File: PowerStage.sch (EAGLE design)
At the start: 97 parts, among them IC1 FSBB30CH60, IC2 HCNR200, IC4 LM358D, IC5 HCNR200, IC6 78L05F, Q1 BC817-16SMD, X1 MKDSN1,5/2-5,08, X2 MKDSN1,5/3-5,08

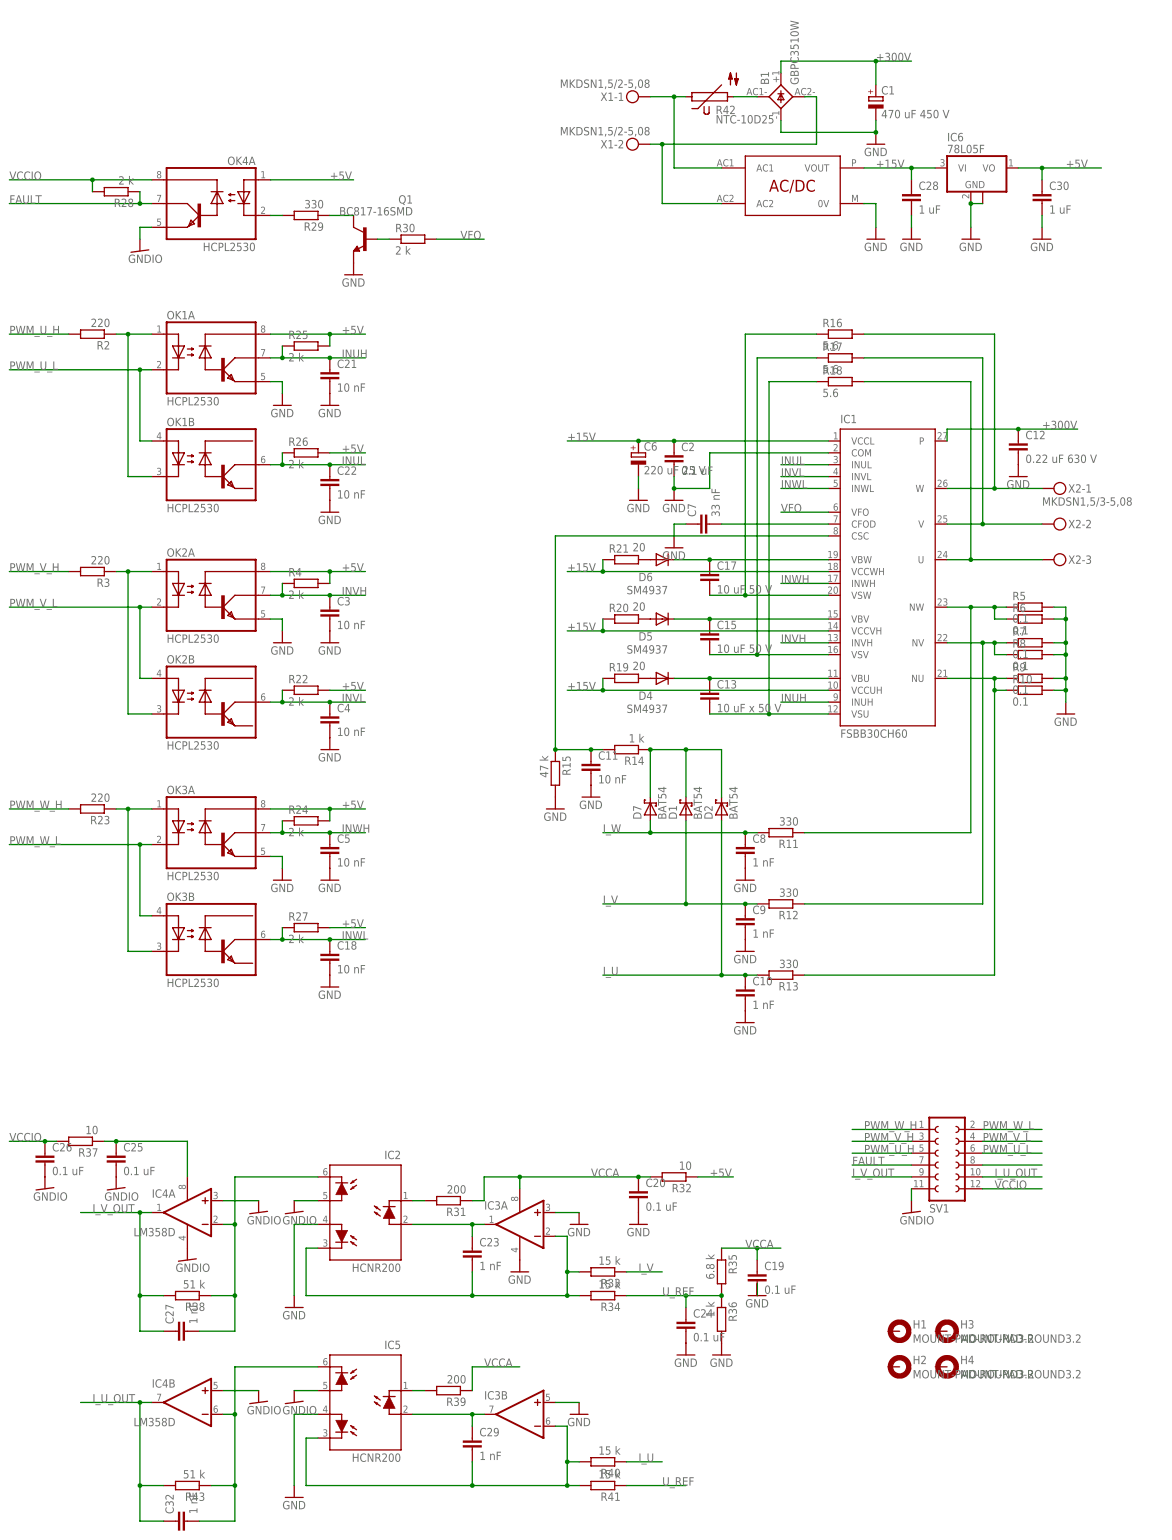
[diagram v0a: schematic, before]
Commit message: Stable version
Tested at  1 kW motor
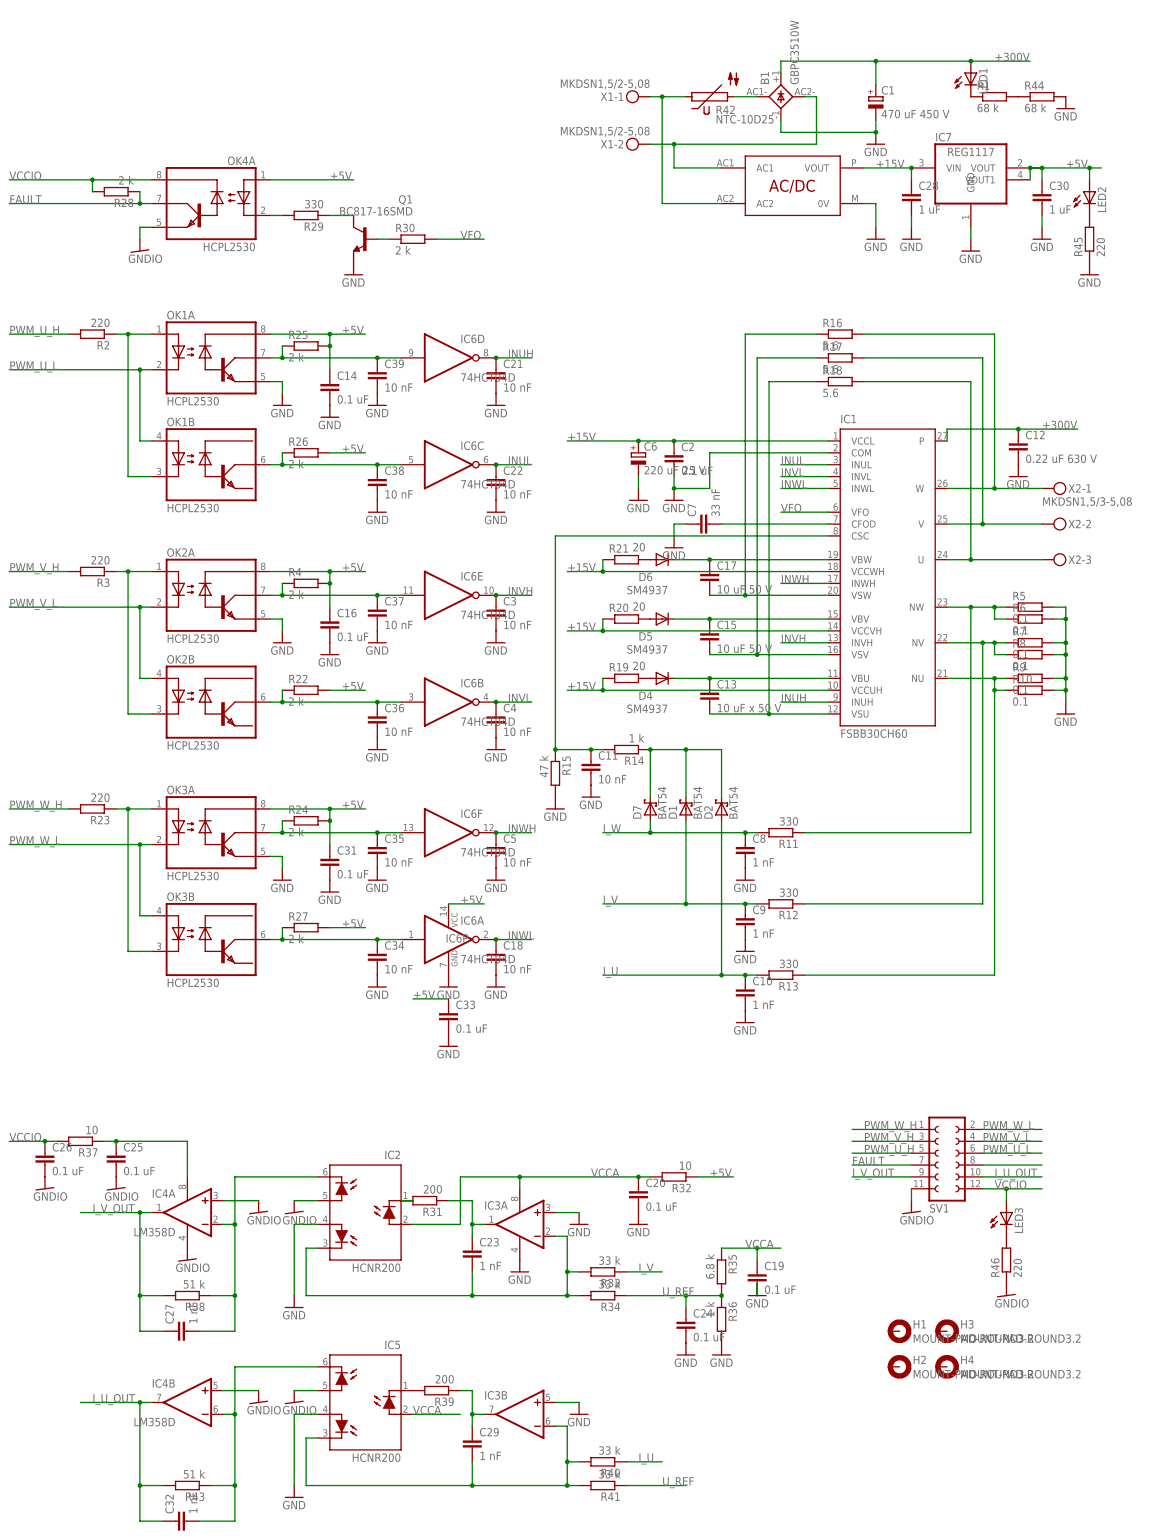
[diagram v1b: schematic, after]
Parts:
- added C14, C16, C31, C33: 0.1 uF, rcl:C-EUC0603
- added C34, C35, C36, C37, C38, C39: 10 nF, rcl:C-EUC0603
- added IC7: REG1117, burr-brown:REG1117
- added LED1, LED2, LED3: (no value), led:LEDCHIP-LED0603
- added R1, R44: 68 k, resistor:R-EU_R1206
- added R45, R46: 220, rcl:R-EU_R0603
- IC6: value 78L05F -> 74HCT04D; device linear:78L05F -> 74xx-eu:74HCT04D
- R33, R34, R40, R41: value 15 k -> 33 k
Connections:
- removed net N$4: B1.AC2, U$1.AC2, X1-2.KL
- new net N$33: C39.1, IC6D.I, OK1A.VO1, R25.1
- new net N$39: C38.1, IC6C.I, OK1B.VO2, R26.1
- new net N$40: C37.1, IC6E.I, OK2A.VO1, R4.1
- new net N$41: C36.1, IC6B.I, OK2B.VO2, R22.1
- new net N$42: C35.1, IC6F.I, OK3A.VO1, R24.1
- new net N$43: C34.1, IC6A.I, OK3B.VO2, R27.1
- new net N$44: LED1.C, R1.1
- new net N$45: R1.2, R44.1
- new net N$46: LED2.C, R45.2
- new net N$47: LED3.C, R46.2
- new net N$48: R42.1, U$1.AC2, X1-1.KL
- net +15V: now also IC7.VIN; no longer IC6.VI
- net +300V: now also LED1.A
- net +5V: now also C14.1, C16.1, C31.1, C33.1, IC6P.VCC, IC7.VOUT, IC7.VOUT1, LED2.A; no longer IC6.VO
- net GND: now also C14.2, C16.2, C31.2, C33.2, C34.2, C35.2, C36.2, C37.2, C38.2, C39.2, IC6P.GND, IC7.GND, R44.2, R45.1; no longer IC6.GND, IC6.GND@1
- net GNDIO: now also R46.1
- net INUH: now also IC6D.O; no longer OK1A.VO1, R25.1
- net INUL: now also IC6C.O; no longer OK1B.VO2, R26.1
- net INVH: now also IC6E.O; no longer OK2A.VO1, R4.1
- net INVL: now also IC6B.O; no longer OK2B.VO2, R22.1
- net INWH: now also IC6F.O; no longer OK3A.VO1, R24.1
- net INWL: now also IC6A.O; no longer OK3B.VO2, R27.1
- net N$35: now also R39.1; no longer IC5.A
- net N$36: now also R31.1; no longer IC2.A
- net N$5: now also B1.AC2, X1-2.KL; no longer R42.1, X1-1.KL
- net VCCA: now also IC2.A, IC5.A; no longer R31.1, R39.1
- net VCCIO: now also LED3.A
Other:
- moved on the sheet: C18, C21, C22, C3, C4, C5, R31, R39
